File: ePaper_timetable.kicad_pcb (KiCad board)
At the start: 2 copper layers, 91.6 x 85.5 mm, 70 parts, among them J1 USB_C_Receptacle_USB2.0, J2 52435-2471, J3 Conn_01x03_Socket, J4 Charging input - 5V, J5 Conn_01x03_Socket, J6 Conn_01x03_Socket, J7 Conn_01x04_Socket, J8 Battery connector, J9 Conn_01x01_Pin, Q1 BSS138, Q2 AO3401A, Q3 FS8205A, Q4 BSS138, SW1 SW_Push, SW2 SW_Push, SW3 SW_Push, SW4 SW_Push, SW5 SW_Push, U1 USBLC6-2SC6, U2 DW01A, U3 TP4056

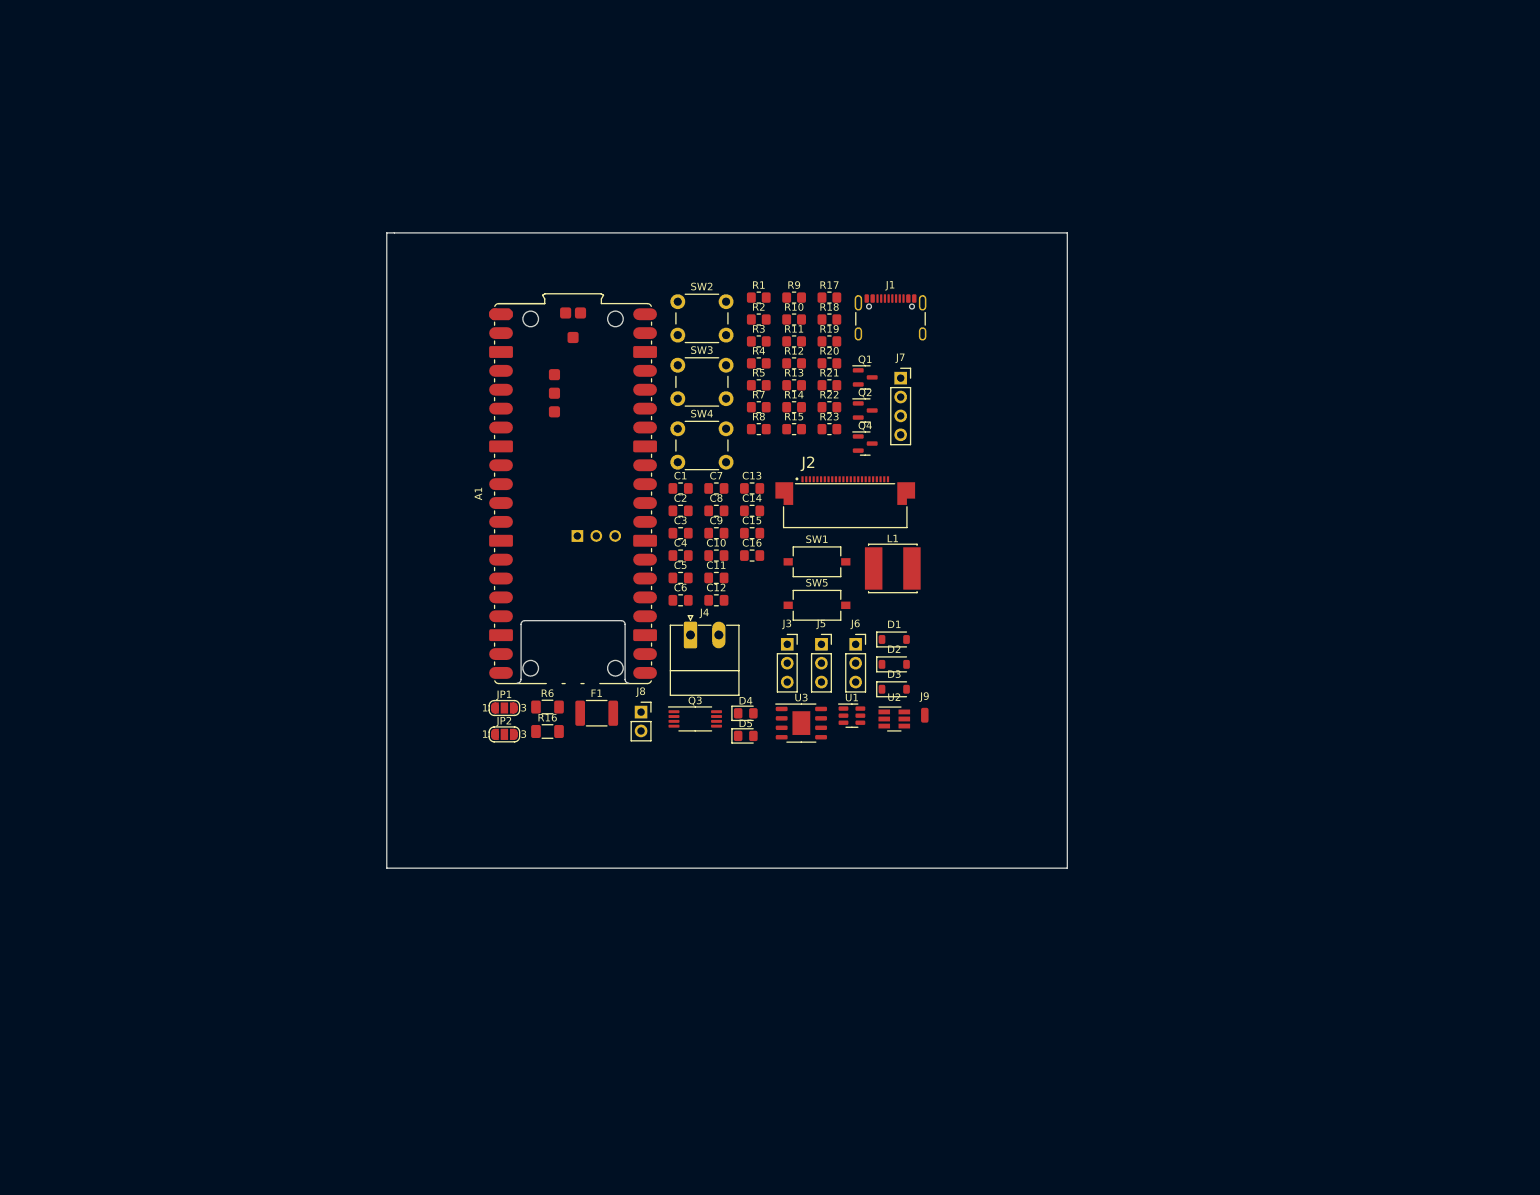
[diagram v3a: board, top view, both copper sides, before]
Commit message: fpc connector fix
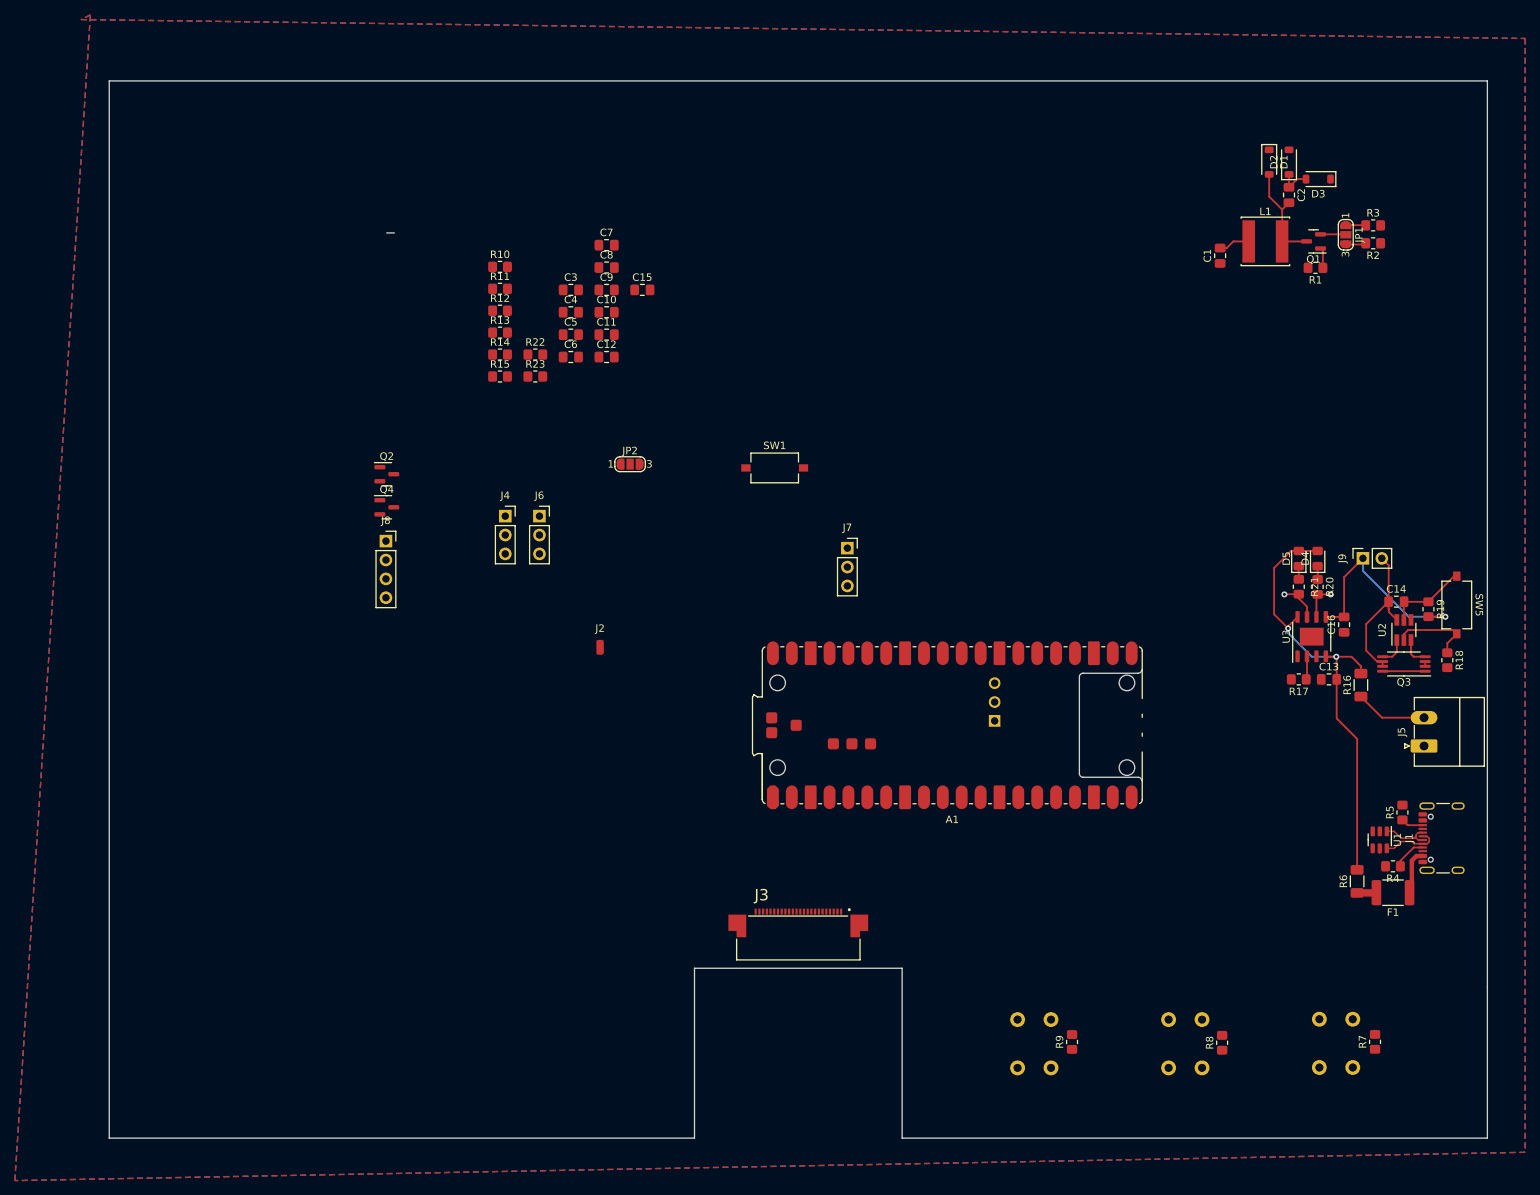
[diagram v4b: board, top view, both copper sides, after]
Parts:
- added REF**: 7_5 inch display, 7_5 inch display model:7_5 inch display, F.Cu at (195.6, 94.0)
- J2: value 52435-2471 -> Conn_01x01_Pin; footprint 52435-2471:MOLEX_52435-2471 -> Connector_Wire:SolderWirePad_1x01_SMD_1x2mm
- J3: value Conn_01x03_Socket -> 52435-2471; footprint Connector_PinSocket_2.54mm:PinSocket_1x03_P2.54mm_Vertical -> 52435-2471:MOLEX_52435-2471
- J4: value Charging input - 5V -> Conn_01x03_Socket; footprint Connector_Phoenix_MC:PhoenixContact_MC_1,5_2-G-3.81_1x02_P3.81mm_Horizontal -> Connector_PinSocket_2.54mm:PinSocket_1x03_P2.54mm_Vertical
- J5: value Conn_01x03_Socket -> Charging input - 5V; footprint Connector_PinSocket_2.54mm:PinSocket_1x03_P2.54mm_Vertical -> Connector_Phoenix_MC:PhoenixContact_MC_1,5_2-G-3.81_1x02_P3.81mm_Horizontal
- J7: value Conn_01x04_Socket -> Conn_01x03_Socket; footprint Connector_PinSocket_2.54mm:PinSocket_1x04_P2.54mm_Vertical -> Connector_PinSocket_2.54mm:PinSocket_1x03_P2.54mm_Vertical
- J8: value Battery connector -> Conn_01x04_Socket; footprint Connector_PinSocket_2.54mm:PinSocket_1x02_P2.54mm_Vertical -> Connector_PinSocket_2.54mm:PinSocket_1x04_P2.54mm_Vertical
- J9: value Conn_01x01_Pin -> Battery connector; footprint Connector_Wire:SolderWirePad_1x01_SMD_1x2mm -> Connector_PinSocket_2.54mm:PinSocket_1x02_P2.54mm_Vertical
- SW2, SW3, SW4: moved to B.Cu
- moved JP1 129.9 mm to (217.2, 46.1), turned to -90 degrees
- moved SW2 129.5 mm to (213.6, 151.6), turned to -90 degrees
- moved R7 119.0 mm to (221.1, 154.7), turned to 90 degrees
- moved R6 111.4 mm to (218.7, 133.1), turned to 90 degrees
- moved SW3 110.1 mm to (193.3, 151.7), turned to -90 degrees
- moved F1 109.8 mm to (223.5, 134.6), turned to 180 degrees
- moved R16 109.6 mm to (219.2, 106.7), turned to 90 degrees
- moved R4 108.9 mm to (223.5, 131.1), turned to 180 degrees
- moved R9 106.9 mm to (180.3, 154.7), turned to 90 degrees
- moved R5 103.9 mm to (224.8, 123.8), turned to 90 degrees
- moved R8 103.5 mm to (200.5, 154.8), turned to 90 degrees
- moved J1 102.1 mm to (231.2, 127.3), turned to 90 degrees
- moved Q3 95.6 mm to (225.0, 103.8), turned to 180 degrees
- moved R18 94.9 mm to (230.8, 103.3), turned to -90 degrees
- moved C2 92.2 mm to (209.5, 40.7), turned to -90 degrees
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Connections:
- net Net-(J1-D+-PadA6) renamed /D+
- net Net-(J1-D--PadA7) renamed /D-
- J2 pad 1: unconnected-(J2-Pad1) -> /BOOTSEL
- J3 pad 1: Net-(J3-Pin_1) -> unconnected-(J3-Pad1)
- J3 pad 2: GND -> /GDR
- J3 pad 3: Net-(J3-Pin_3) -> /RESE
- J4 pad 1: GND -> Net-(J4-Pin_1)
- J4 pad 2: Net-(J4-Pin_2) -> GND
- J5 pad 1: Net-(J5-Pin_1) -> GND
- J5 pad 2: GND -> Net-(J5-Pin_2)
- J6 pad 1: Net-(J3-Pin_1) -> Net-(J6-Pin_1)
- J6 pad 3: Net-(J3-Pin_3) -> Net-(J6-Pin_3)
- J7 pad 1: +3V3 -> Net-(J4-Pin_1)
- J7 pad 2: /I2C0_SDA -> GND
- J7 pad 3: /I2C0_SCL -> Net-(J4-Pin_3)
- J8 pad 1: +BATT -> +3V3
- J8 pad 2: -BATT -> /I2C0_SDA
- J9 pad 1: /BOOTSEL -> +BATT
- R10 pad 1: Net-(J3-Pin_1) -> Net-(J4-Pin_1)
- R11 pad 1: Net-(J3-Pin_3) -> Net-(J4-Pin_3)
- R13 pad 1: Net-(J5-Pin_1) -> Net-(J6-Pin_1)
- R14 pad 1: Net-(J5-Pin_3) -> Net-(J6-Pin_3)
- R16 pad 1: Net-(J4-Pin_2) -> Net-(J5-Pin_2)
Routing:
- net +5V: track 0.00 -> 62.6 mm, vias 0 -> 2
- net +BATT: track 0.00 -> 29.0 mm, vias 0 -> 1
- net -BATT: track 0.00 -> 20.4 mm
- net Net-(D1-A): track 0.00 -> 14.3 mm
- net Net-(U2-CS): track 0.00 -> 11.4 mm
- net /DW01_{Vcc}: track 0.00 -> 10.6 mm
- net Net-(J5-Pin_2): track 0.00 -> 9.67 mm
- net /D-: track 0.00 -> 7.77 mm
- net /D+: track 0.00 -> 7.18 mm
- net Net-(F1-Pad1): track 0.00 -> 5.92 mm
- net unconnected-(Q3-Pad1): track 0.00 -> 5.73 mm
- net /BAT_CHRG: track 0.00 -> 5.46 mm, vias 0 -> 1
- net /BAT_STDBY: track 0.00 -> 4.87 mm, vias 0 -> 1
- net Net-(J1-CC1): track 0.00 -> 4.49 mm
- net Net-(D2-K): track 0.00 -> 4.48 mm
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- added copper zone on B.Cu, net GND
- added copper zone on F.Cu, net GND
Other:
- board size 91.6 x 85.5 mm -> 185.4 x 142.2 mm

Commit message: layout started
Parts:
- moved C7 91.2 mm to (147.4, 133.7), turned to -90 degrees
- moved C8 87.4 mm to (144.8, 133.6), turned to -90 degrees
- moved C5 83.3 mm to (149.6, 134.4), turned to -90 degrees
- moved C3 81.8 mm to (138.7, 131.2), turned to -90 degrees
- moved C4 80.9 mm to (140.7, 132.5), turned to -90 degrees
- moved C9 80.8 mm to (133.5, 132.7)
- moved C10 79.7 mm to (133.2, 134.7)
- moved C11 78.2 mm to (142.7, 133.6), turned to -90 degrees
- moved C12 76.6 mm to (132.5, 137.7), turned to 90 degrees
- moved JP2 73.7 mm to (156.0, 141.7), turned to 90 degrees
- moved C6 72.6 mm to (136.7, 131.2), turned to -90 degrees
- moved J8 70.7 mm to (118.1, 151.3)
- moved Q2 52.5 mm to (140.0, 86.7), turned to 90 degrees
- moved J7 29.0 mm to (121.2, 90.6)
- moved SW1 24.7 mm to (164.2, 83.8), turned to 90 degrees
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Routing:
- net /BS: track 0.00 -> 13.3 mm
- net Net-(C9-Pad2): track 0.00 -> 6.55 mm
- net /VGH: track 0.00 -> 6.02 mm
- net Net-(C12-Pad2): track 0.00 -> 5.53 mm
- net Net-(C3-Pad2): track 0.00 -> 5.38 mm
- net /VGL: track 0.00 -> 5.31 mm
- net +3V3: track 4.21 -> 8.66 mm
- net Net-(C4-Pad2): track 0.00 -> 3.85 mm
- net Net-(C11-Pad2): track 0.00 -> 3.34 mm
- net Net-(C5-Pad2): track 0.00 -> 2.94 mm
- net Net-(C7-Pad2): track 0.00 -> 2.46 mm

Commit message: layout proposition
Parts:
- moved R10 212.9 mm to (282.9, 164.8)
- moved R13 202.6 mm to (276.1, 165.1)
- moved R14 191.6 mm to (268.0, 160.4)
- moved R15 191.4 mm to (277.9, 143.9)
- moved R11 187.9 mm to (268.1, 143.9)
- moved R12 185.2 mm to (263.0, 150.2)
- moved J6 182.7 mm to (279.1, 149.6)
- moved J4 182.4 mm to (274.1, 150.2)
- moved J1 180.5 mm to (50.7, 130.2), turned to -90 degrees
- moved J5 177.0 mm to (55.0, 153.8), turned to -90 degrees
- moved J7 172.2 mm to (283.0, 149.6)
- moved J8 170.5 mm to (288.7, 149.2)
- moved R5 167.9 mm to (57.1, 133.7), turned to -90 degrees
- moved F1 165.6 mm to (58.4, 121.6), turned to 0 degrees
- moved R4 165.2 mm to (58.4, 126.4), turned to 0 degrees
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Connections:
- net /USB_DM renamed /USB-
- net /USB_DP renamed /USB+
- Q3 pad 1: unconnected-(Q3-Pad1) -> /Interconnect
- Q3 pad 8: unconnected-(Q3-Pad1) -> /Interconnect
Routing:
- net +3V3: track 8.66 -> 203.6 mm, vias 0 -> 6
- net /SW3: track 0.00 -> 134.4 mm
- net /SW2: track 0.00 -> 111.0 mm
- net /SW1: track 0.00 -> 98.7 mm
- net +BATT: track 29.0 -> 101.2 mm, vias 1 -> 2
- net +5V: track 62.6 -> 130.9 mm
- net /EPD_DC': track 0.00 -> 52.9 mm, vias 0 -> 2
- net /EPD_CS': track 0.00 -> 49.9 mm, vias 0 -> 2
- net /EPD_SCK': track 0.00 -> 45.3 mm, vias 0 -> 2
- net /EPD_RST': track 0.00 -> 43.9 mm, vias 0 -> 2
- net /GDR: track 2.74 -> 45.0 mm, vias 0 -> 2
- net /EPD_BUSY': track 0.00 -> 42.2 mm, vias 0 -> 2
- net /EPD_DIN': track 0.00 -> 41.8 mm, vias 0 -> 2
- net /USB+: track 0.00 -> 40.3 mm, vias 0 -> 2
- net /USB-: track 0.00 -> 40.3 mm, vias 0 -> 2
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- added copper zone on F.Cu, net -BATT
- added copper zone on F.Cu, net /GDR
- added copper zone on F.Cu, net /Interconnect
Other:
- board size 185.4 x 142.2 mm -> 191.8 x 144.8 mm

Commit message: layout started
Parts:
- moved REF** 188.4 mm to (377.2, 143.5)
- moved J6 174.8 mm to (106.9, 119.8), turned to -90 degrees
- moved J8 174.4 mm to (115.3, 130.3), turned to 180 degrees
- moved R13 170.8 mm to (111.5, 119.4)
- moved R14 166.5 mm to (107.6, 115.7)
- moved R15 166.1 mm to (112.4, 128.9), turned to -90 degrees
- moved R12 153.6 mm to (111.4, 125.5), turned to 180 degrees
- moved J7 99.0 mm to (207.0, 86.0)
- moved R10 97.7 mm to (217.6, 92.2)
- moved R9 94.0 mm to (127.0, 150.5)
- moved SW4 83.4 mm to (130.3, 149.2)
- moved SW3 83.1 mm to (110.3, 149.2)
- moved R8 83.1 mm to (117.6, 150.4)
- moved R7 82.8 mm to (97.6, 150.6)
- moved SW2 82.8 mm to (90.2, 149.2)
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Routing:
- net +3V3: track 203.6 -> 155.5 mm, vias 6 -> 2
- net +BATT: track 101.2 -> 56.2 mm
- net /SW3: track 134.4 -> 90.4 mm, vias 0 -> 1
- net /SW2: track 111.0 -> 80.3 mm, vias 0 -> 1
- net /BAT_CHRG: track 37.0 -> 61.1 mm
- net /I2C0_SDA: track 0.00 -> 21.6 mm, vias 0 -> 1
- net /I2C0_SCL: track 0.00 -> 20.4 mm, vias 0 -> 1
- net /BAT_STDBY: track 33.0 -> 51.5 mm
- net /EPD_CS': track 49.9 -> 32.7 mm
- net /EPD_RST': track 43.9 -> 26.8 mm
- net /EPD_SCK': track 45.3 -> 28.7 mm
- net /EPD_DIN': track 41.8 -> 25.4 mm
- net /USB-: track 40.3 -> 56.4 mm, vias 2 -> 0
- net /USB+: track 40.3 -> 56.3 mm, vias 2 -> 0
- net /EPD_BUSY': track 42.2 -> 26.3 mm
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- added copper zone on F.Cu, net Net-(D1-A)
- added copper zone on F.Cu, net Net-(D2-K)
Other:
- board size 191.8 x 144.8 mm -> 95.2 x 80.6 mm

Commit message: prepared for review
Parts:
- added G***: LOGO, buczkolo:kne, F.Cu at (106.0, 83.4)
- moved J4 82.6 mm to (143.5, 83.2), turned to 90 degrees
- moved R10 77.6 mm to (140.0, 89.4), turned to -90 degrees
- moved REF** 66.5 mm to (320.9, 108.1)
- moved R11 63.6 mm to (152.0, 89.6), turned to -90 degrees
- moved J7 63.6 mm to (143.5, 88.9), turned to 90 degrees
- moved SW1 8.80 mm to (132.4, 85.7), turned to 90 degrees
- moved SW5 2.18 mm to (106.7, 93.6)
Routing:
- net /SWCLK: track 0.00 -> 16.3 mm, vias 0 -> 1
- net /SWDIO: track 0.00 -> 14.0 mm, vias 0 -> 1
- net Net-(J4-Pin_1): track 0.00 -> 9.39 mm
- net Net-(J4-Pin_3): track 0.00 -> 9.30 mm
- net +BATT: track 56.2 -> 48.9 mm, vias 2 -> 1
- net /EPD_RST': track 26.8 -> 29.0 mm
- net Net-(U2-CS): track 11.3 -> 13.4 mm
- net Net-(A1-RUN): track 6.59 -> 8.52 mm
- net /DW01_{Vcc}: track 10.2 -> 12.1 mm
- net /EPD_DC': track 37.8 -> 36.3 mm
- net -BATT: track 21.9 -> 21.2 mm
- net /EPD_CS': track 32.7 -> 33.2 mm
- net +3V3: track 155.5 -> 156.0 mm
- net GND: vias 0 -> 96
